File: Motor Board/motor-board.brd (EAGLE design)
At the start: 60 x 23 mm, 13 parts

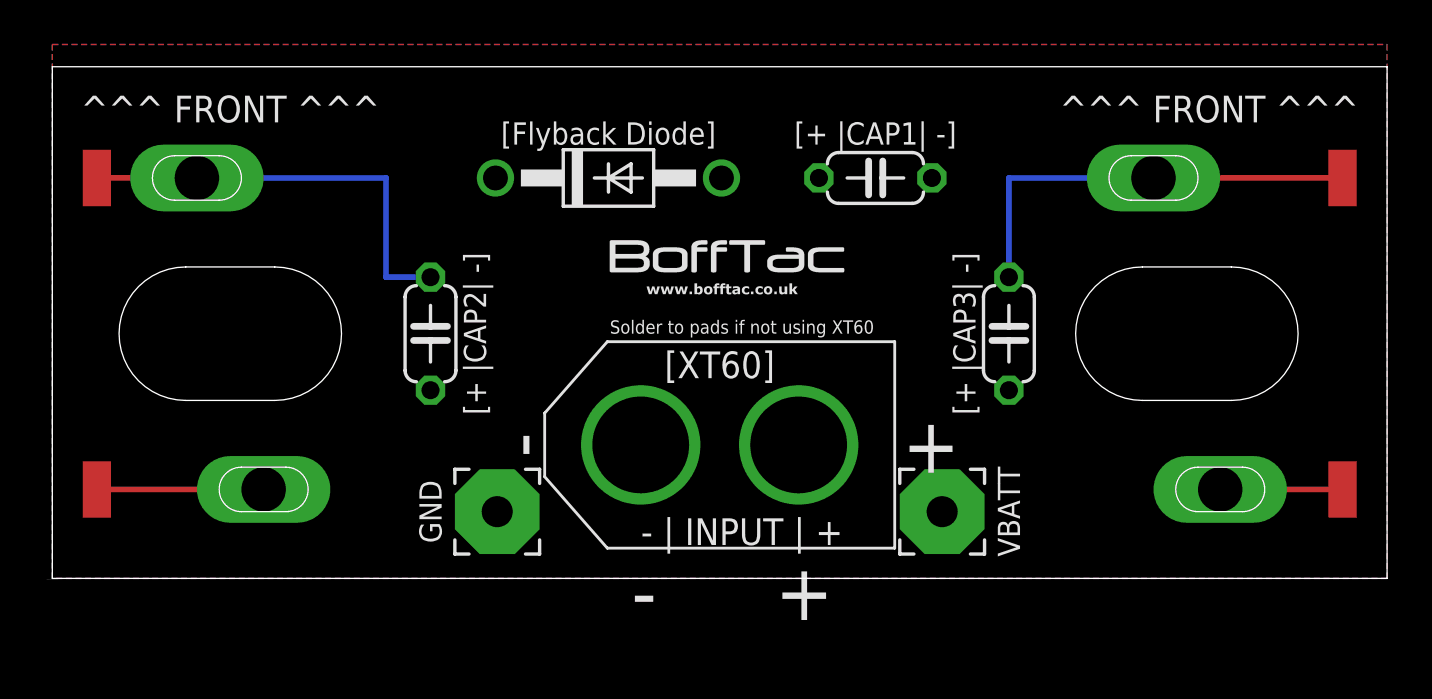
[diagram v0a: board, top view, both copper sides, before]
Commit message: Spacing Update
Updated the motor terminal spacing on the EAGLE files in order to hopefully get it right the third time.
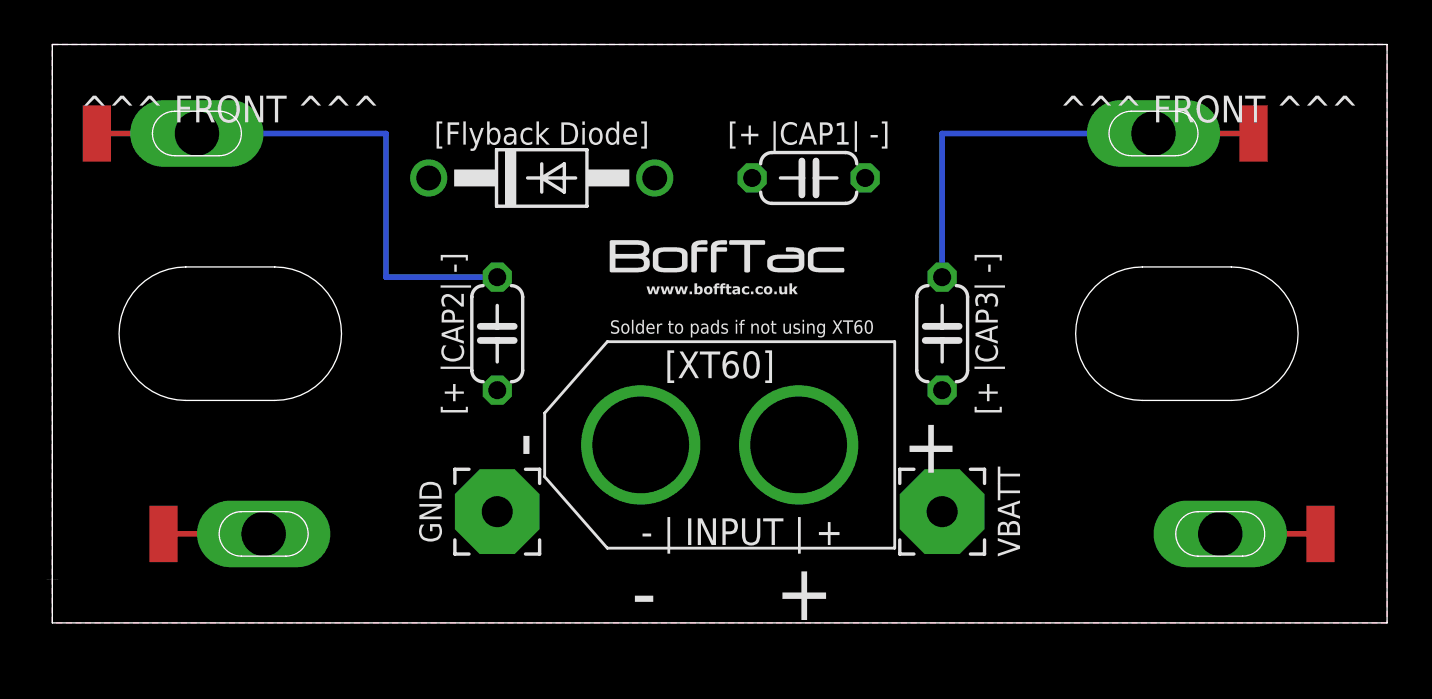
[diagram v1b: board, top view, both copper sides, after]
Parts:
- moved PAD4 4.47 mm to (54.0, 20.0)
- moved TOP-CAN 3.61 mm to (5.00, 2.00)
- moved C1 3.00 mm to (34.0, 18.0)
- moved C2 3.00 mm to (40.0, 11.0)
- moved C3 3.00 mm to (20.0, 11.0)
- moved D1 3.00 mm to (22.0, 18.0)
- moved BOTTOM-CAN 2.24 mm to (57.0, 2.00)
- moved PAD1 2.00 mm to (2.00, 20.0)
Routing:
- net GND: track 38.9 -> 44.9 mm
- net VBATT: track 13.0 -> 9.00 mm
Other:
- board size 60 x 23 mm -> 60 x 26 mm
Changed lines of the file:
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@@
 <setting verticaltext="up"/>
 </settings>
-<grid distance="100" unitdist="mil" unit="mil" style="lines" multiple="1" display="yes" altdistance="10" altunitdist="mil" altunit="mil"/>
+<grid distance="1" unitdist="mm" unit="mm" style="lines" multiple="1" display="yes" altdistance="0.5" altunitdist="mm" altunit="mm"/>
 <layers>
 <layer number="1" name="Top" color="4" fill="1" visible="yes" active="yes"/>
@@
 <board>
 <plain>
-<wire x1="0" y1="0" x2="60" y2="0" width="0" layer="20"/>
-<wire x1="60" y1="0" x2="60" y2="23" width="0" layer="20"/>
-<wire x1="0" y1="23" x2="0" y2="0" width="0" layer="20"/>
-<wire x1="0" y1="23" x2="60" y2="23" width="0" layer="20"/>
-<text x="19" y="11" size="1" layer="25" ratio="12" rot="R90" align="center">[+ |CAP2| -]</text>
-<text x="25" y="19.5" size="1" layer="25" ratio="12" align="bottom-center">[Flyback Diode]</text>
-<text x="37" y="20" size="1" layer="25" ratio="12" rot="R180" align="center">[+ |CAP1| -]</text>
-<text x="41" y="11" size="1" layer="25" ratio="12" rot="R270" align="center">[+ |CAP3| -]</text>
+<wire x1="0" y1="-2" x2="60" y2="-2" width="0" layer="20"/>
+<wire x1="60" y1="-2" x2="60" y2="24" width="0" layer="20"/>
+<wire x1="0" y1="24" x2="0" y2="-2" width="0" layer="20"/>
+<wire x1="0" y1="24" x2="60" y2="24" width="0" layer="20"/>
+<text x="18" y="11" size="1" layer="25" ratio="12" rot="R90" align="center">[+ |CAP2| -]</text>
+<text x="22" y="19.5" size="1" layer="25" ratio="12" align="bottom-center">[Flyback Diode]</text>
+<text x="34" y="20" size="1" layer="25" ratio="12" rot="R180" align="center">[+ |CAP1| -]</text>
+<text x="42" y="11" size="1" layer="25" ratio="12" rot="R270" align="center">[+ |CAP3| -]</text>
 <text x="8" y="20.5" size="1.2" layer="25" ratio="12" align="bottom-center">^^^ FRONT ^^^</text>
 <text x="52" y="20.5" size="1.2" layer="25" ratio="12" align="bottom-center">^^^ FRONT ^^^</text>
@@
 <attribute name="VALUE" x="37.8675" y="10.94" size="1.27" layer="27" align="bottom-right"/>
 </element>
-<element name="C1" library="resistor" package="C050-024X044" value="" x="37" y="18" smashed="yes">
-<attribute name="VALUE" x="34.841" y="15.333" size="1.27" layer="27" ratio="10"/>
+<element name="C1" library="resistor" package="C050-024X044" value="" x="34" y="18" smashed="yes">
+<attribute name="VALUE" x="31.841" y="15.333" size="1.27" layer="27" ratio="10"/>
 </element>
-<element name="D1" library="diode" package="DO41-10" value="RGP10" x="25" y="18" smashed="yes"/>
-<element name="C2" library="resistor" package="C050-024X044" value="" x="43" y="11" smashed="yes" rot="R90">
-<attribute name="VALUE" x="45.667" y="8.841" size="1.27" layer="27" ratio="10" rot="R90"/>
+<element name="D1" library="diode" package="DO41-10" value="RGP10" x="22" y="18" smashed="yes"/>
+<element name="C2" library="resistor" package="C050-024X044" value="" x="40" y="11" smashed="yes" rot="R90">
+<attribute name="VALUE" x="42.667" y="8.841" size="1.27" layer="27" ratio="10" rot="R90"/>
 </element>
-<element name="C3" library="resistor" package="C050-024X044" value="" x="17" y="11" smashed="yes" rot="R90">
-<attribute name="VALUE" x="19.667" y="8.841" size="1.27" layer="27" ratio="10" rot="R90"/>
+<element name="C3" library="resistor" package="C050-024X044" value="" x="20" y="11" smashed="yes" rot="R90">
+<attribute name="VALUE" x="22.667" y="8.841" size="1.27" layer="27" ratio="10" rot="R90"/>
 </element>
-<element name="PAD1" library="wirepad" package="SMD1,27-2,54" value="" x="2" y="18" smashed="yes">
-<attribute name="VALUE" x="2" y="18" size="0.0254" layer="27"/>
+<element name="PAD1" library="wirepad" package="SMD1,27-2,54" value="" x="2" y="20" smashed="yes">
+<attribute name="VALUE" x="2" y="20" size="0.0254" layer="27"/>
 </element>
-<element name="TOP-CAN" library="wirepad" package="SMD1,27-2,54" value="" x="2" y="4" smashed="yes">
-<attribute name="VALUE" x="2" y="4" size="0.0254" layer="27"/>
+<element name="TOP-CAN" library="wirepad" package="SMD1,27-2,54" value="" x="5" y="2" smashed="yes">
+<attribute name="VALUE" x="5" y="2" size="0.0254" layer="27"/>
 </element>
-<element name="BOTTOM-CAN" library="wirepad" package="SMD1,27-2,54" value="" x="58" y="4" smashed="yes" rot="R180">
-<attribute name="VALUE" x="58" y="4" size="0.0254" layer="27" rot="R180"/>
+<element name="BOTTOM-CAN" library="wirepad" package="SMD1,27-2,54" value="" x="57" y="2" smashed="yes" rot="R180">
+<attribute name="VALUE" x="57" y="2" size="0.0254" layer="27" rot="R180"/>
 </element>
-<element name="PAD4" library="wirepad" package="SMD1,27-2,54" value="" x="58" y="18" smashed="yes" rot="R180">
-<attribute name="VALUE" x="58" y="18" size="0.0254" layer="27" rot="R180"/>
+<element name="PAD4" library="wirepad" package="SMD1,27-2,54" value="" x="54" y="20" smashed="yes" rot="R180">
+<attribute name="VALUE" x="54" y="20" size="0.0254" layer="27" rot="R180"/>
 </element>
 <element name="U$1" library="130-can" package="130-MOTOR-CAN" value="130-CAN-DEVICE130-MOTOR-CAN" x="7.5" y="11" rot="MR90"/>
@@
 <vertex x="0" y="24"/>
 <vertex x="60" y="24"/>
-<vertex x="60" y="0"/>
-<vertex x="0" y="0"/>
+<vertex x="60" y="-2"/>
+<vertex x="0" y="-2"/>
 </polygon>
 <contactref element="U$2" pad="MOTOR-VE"/>
@@
 <contactref element="PAD4" pad="1"/>
 <contactref element="PAD1" pad="1"/>
-<wire x1="49.5" y1="18" x2="43" y2="18" width="0.254" layer="16"/>
-<wire x1="43" y1="18" x2="43" y2="13.54" width="0.254" layer="16"/>
-<wire x1="58" y1="18" x2="49.5" y2="18" width="0.254" layer="1"/>
-<wire x1="17" y1="13.54" x2="15" y2="13.54" width="0.254" layer="16"/>
-<wire x1="15" y1="13.54" x2="15" y2="18" width="0.254" layer="16"/>
-<wire x1="15" y1="18" x2="6.5" y2="18" width="0.254" layer="16"/>
+<wire x1="49.5" y1="20" x2="40" y2="20" width="0.254" layer="16"/>
+<wire x1="40" y1="20" x2="40" y2="13.54" width="0.254" layer="16"/>
+<wire x1="54" y1="20" x2="49.5" y2="20" width="0.254" layer="1"/>
+<wire x1="20" y1="13.54" x2="15" y2="13.54" width="0.254" layer="16"/>
+<wire x1="15" y1="13.54" x2="15" y2="20" width="0.254" layer="16"/>
+<wire x1="15" y1="20" x2="6.5" y2="20" width="0.254" layer="16"/>
 <contactref element="D1" pad="A"/>
-<wire x1="2" y1="18" x2="6.5" y2="18" width="0.254" layer="1"/>
+<wire x1="2" y1="20" x2="6.5" y2="20" width="0.254" layer="1"/>
 <contactref element="PAD-GND" pad="1"/>
 </signal>
@@
 <vertex x="0" y="24"/>
 <vertex x="60" y="24"/>
-<vertex x="60" y="0"/>
-<vertex x="0" y="0"/>
+<vertex x="60" y="-2"/>
+<vertex x="0" y="-2"/>
 </polygon>
 <contactref element="J1" pad="+"/>
@@
 <contactref element="BOTTOM-CAN" pad="1"/>
 <contactref element="TOP-CAN" pad="1"/>
-<wire x1="2" y1="4" x2="9.5" y2="4" width="0.254" layer="1"/>
-<wire x1="58" y1="4" x2="52.5" y2="4" width="0.254" layer="1"/>
+<wire x1="5" y1="2" x2="9.5" y2="2" width="0.254" layer="1"/>
+<wire x1="57" y1="2" x2="52.5" y2="2" width="0.254" layer="1"/>
 <contactref element="D1" pad="C"/>
 <contactref element="PAD-VBATT" pad="1"/>
